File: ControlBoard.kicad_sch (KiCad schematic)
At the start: 9 parts, among them J1 Conn_02x07_Odd_Even, J2 Conn_02x07_Odd_Even, J3 Conn_02x03_Odd_Even, J5 Conn_01x06, J6 Conn_01x06, J7 Conn_01x02

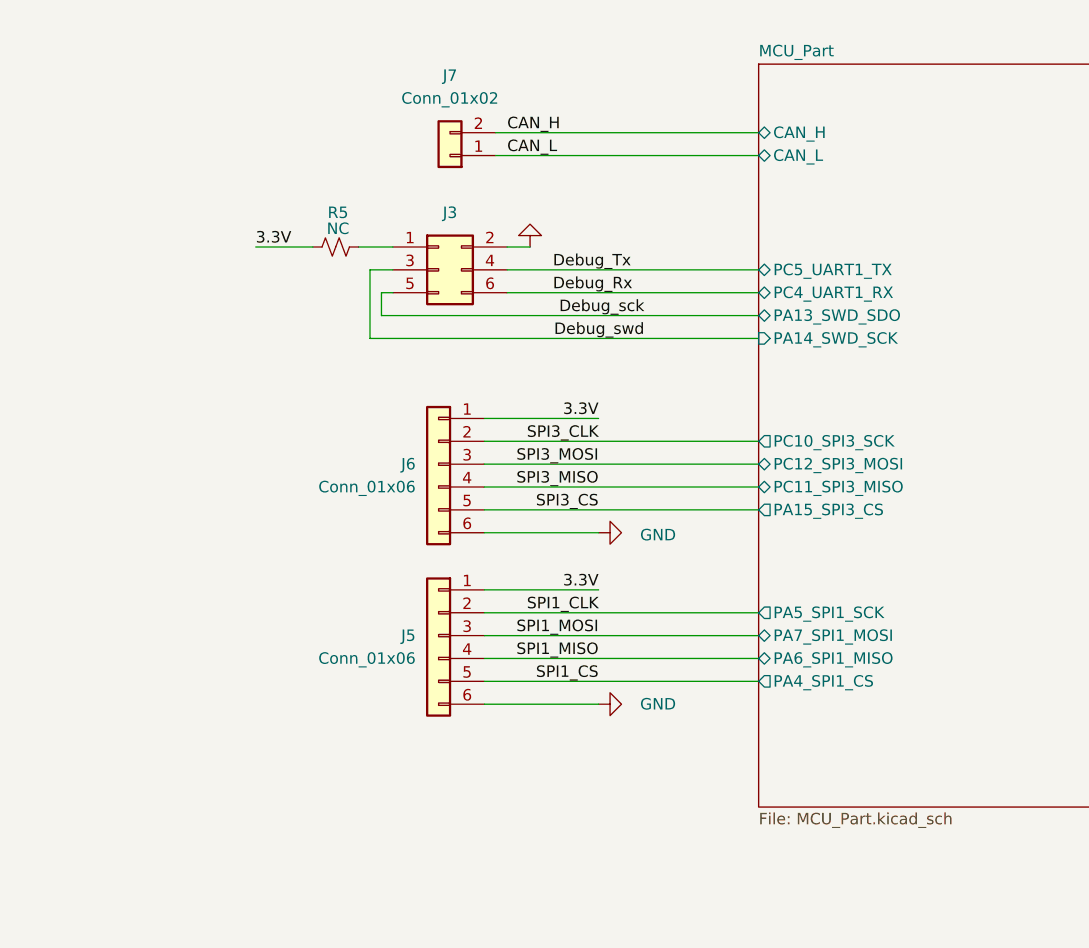
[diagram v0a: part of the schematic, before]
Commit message: 重新分配端子封装
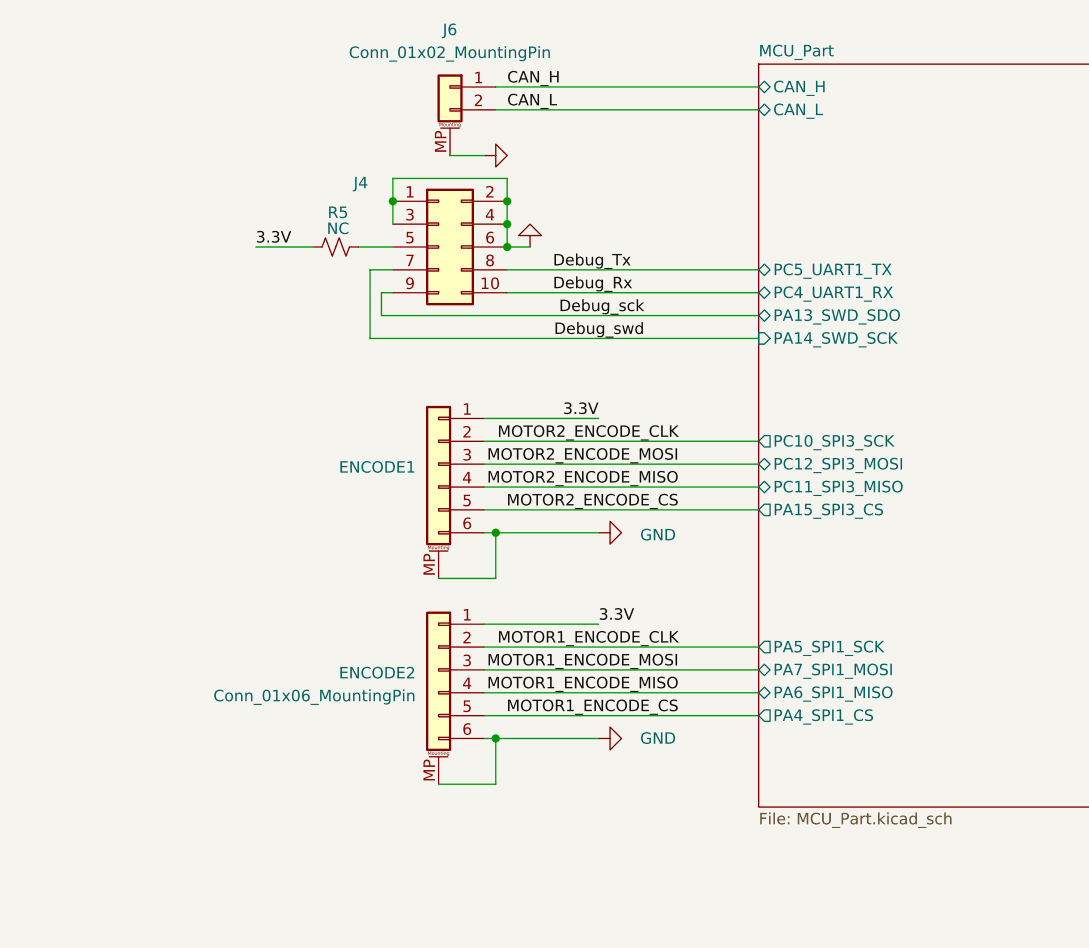
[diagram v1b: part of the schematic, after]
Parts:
- removed J3: Conn_02x03_Odd_Even, Connector_IDC:IDC-Header_2x03_P2.54mm_Vertical_SMD, symbol Connector_Generic:Conn_02x03_Odd_Even
- removed J5, J6: Conn_01x06, Connector_JST:JST_SH_BM06B-SRSS-TB_1x06-1MP_P1.00mm_Vertical, symbol Connector_Generic:Conn_01x06
- removed J7: Conn_01x02, Connector_JST:JST_SH_BM02B-SRSS-TB_1x02-1MP_P1.00mm_Vertical, symbol Connector_Generic:Conn_01x02
- added ENCODE1: ENCODE1, footprints:JST_SH_BM06B-SRSS-TB_1x06-1MP_P1.00mm_Horizontal, symbol Connector_Generic_MountingPin:Conn_01x06_MountingPin
- added ENCODE2: Conn_01x06_MountingPin, footprints:JST_SH_BM06B-SRSS-TB_1x06-1MP_P1.00mm_Horizontal, symbol Connector_Generic_MountingPin:Conn_01x06_MountingPin
- added J4: Conn_02x05_Odd_Even, footprints:Box_Head_1.27mm_SMD_Vertical_02x05, symbol Connector_Generic:Conn_02x05_Odd_Even
- added J6: Conn_01x02_MountingPin, footprints:JST_SH_BM02B-SRSS-TB_1x02-1MP_P1.00mm_Horizontal, symbol Connector_Generic_MountingPin:Conn_01x02_MountingPin
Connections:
- net 3.3V: now also ENCODE1.1 (Pin_1), ENCODE2.1 (Pin_1)
- net CAN_H: now also J6.1 (Pin_1)
- net CAN_L: now also J6.2 (Pin_2)
- net Debug_Rx: now also J4.10 (Pin_10)
- net Debug_Tx: now also J4.8 (Pin_8)
- net Debug_sck: now also J4.9 (Pin_9)
- net Debug_swd: now also J4.7 (Pin_7)
- net GND: now also ENCODE1.6 (Pin_6), ENCODE1.MP (MountPin), ENCODE2.6 (Pin_6), ENCODE2.MP (MountPin), J4.1 (Pin_1), J4.2 (Pin_2), J4.3 (Pin_3), J4.4 (Pin_4), J4.6 (Pin_6), J6.MP (MountPin)
- net at R5.2: now also J4.5 (Pin_5)
- new net MOTOR1_ENCODE_CLK: ENCODE2.2 (Pin_2)
- new net MOTOR1_ENCODE_CS: ENCODE2.5 (Pin_5)
- new net MOTOR1_ENCODE_MISO: ENCODE2.4 (Pin_4)
- new net MOTOR1_ENCODE_MOSI: ENCODE2.3 (Pin_3)
- new net MOTOR2_ENCODE_CLK: ENCODE1.2 (Pin_2)
- new net MOTOR2_ENCODE_CS: ENCODE1.5 (Pin_5)
- new net MOTOR2_ENCODE_MISO: ENCODE1.4 (Pin_4)
- new net MOTOR2_ENCODE_MOSI: ENCODE1.3 (Pin_3)

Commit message: 增加测试点
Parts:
- added TP10, TP11, TP12, TP13, TP14, TP15, TP16, TP17, TP18, TP19, TP20, TP21, TP22, TP23, TP24, TP25, TP26, TP27, TP28, TP29, TP3, TP30, TP31, TP32, TP33, TP34, TP35, TP36, TP37, TP38, TP39, TP4, TP40, TP41, TP42, TP43, TP44, TP45, TP46, TP47, TP48, TP5, TP6, TP7, TP8, TP9: TestPoint_Small, TestPoint:TestPoint_Pad_D1.0mm, symbol Connector:TestPoint_Small
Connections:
- net +3.3V: now also TP48.1
- net +5V: now also TP47.1
- net BusVoltage: now also TP22.1
- net CAN_H: now also J6.2 (Pin_2), TP4.1; no longer J6.1 (Pin_1)
- net CAN_L: now also J6.1 (Pin_1), TP3.1; no longer J6.2 (Pin_2)
- net MOTOR1_ADC_U: now also TP19.1
- net MOTOR1_ADC_V: now also TP20.1
- net MOTOR1_ADC_W: now also TP21.1
- net MOTOR1_BREAK: now also TP24.1
- net MOTOR1_ENCODE_CLK: now also TP9.1
- net MOTOR1_ENCODE_CS: now also TP12.1
- net MOTOR1_ENCODE_MISO: now also TP11.1
- net MOTOR1_ENCODE_MOSI: now also TP10.1
- net MOTOR1_U+: now also TP13.1, TP25.1
- net MOTOR1_U-: now also TP14.1, TP18.1, TP26.1, TP30.1
- net MOTOR1_V+: now also TP15.1, TP27.1
- net MOTOR1_V-: now also TP16.1, TP28.1
- net MOTOR1_W+: now also TP17.1, TP29.1
- net MOTOR2_ADC_U: now also TP37.1
- net MOTOR2_ADC_V: now also TP38.1
- net MOTOR2_ADC_W: now also TP39.1
- net MOTOR2_BREAK: now also TP40.1
- net MOTOR2_ENCODE_CLK: now also TP5.1
- net MOTOR2_ENCODE_CS: now also TP8.1
- net MOTOR2_ENCODE_MISO: now also TP7.1
- net MOTOR2_ENCODE_MOSI: now also TP6.1
- net MOTOR2_U+: now also TP31.1, TP41.1
- net MOTOR2_U-: now also TP32.1, TP36.1, TP42.1, TP46.1
- net MOTOR2_V+: now also TP33.1, TP43.1
- net MOTOR2_V-: now also TP34.1, TP44.1
- net MOTOR2_W+: now also TP35.1, TP45.1
- net busCurrent: now also TP23.1

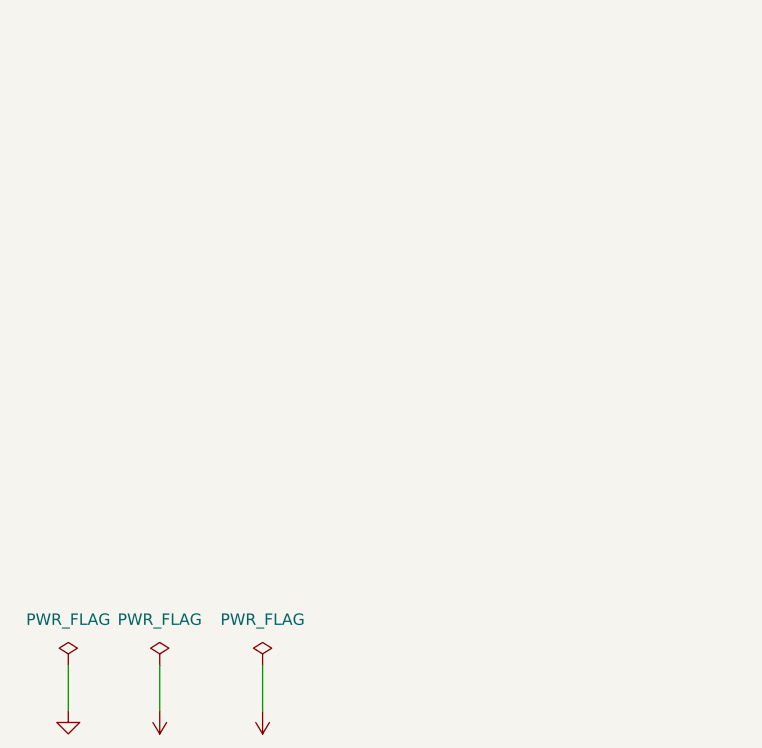
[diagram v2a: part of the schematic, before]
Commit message: 增加typeC接口
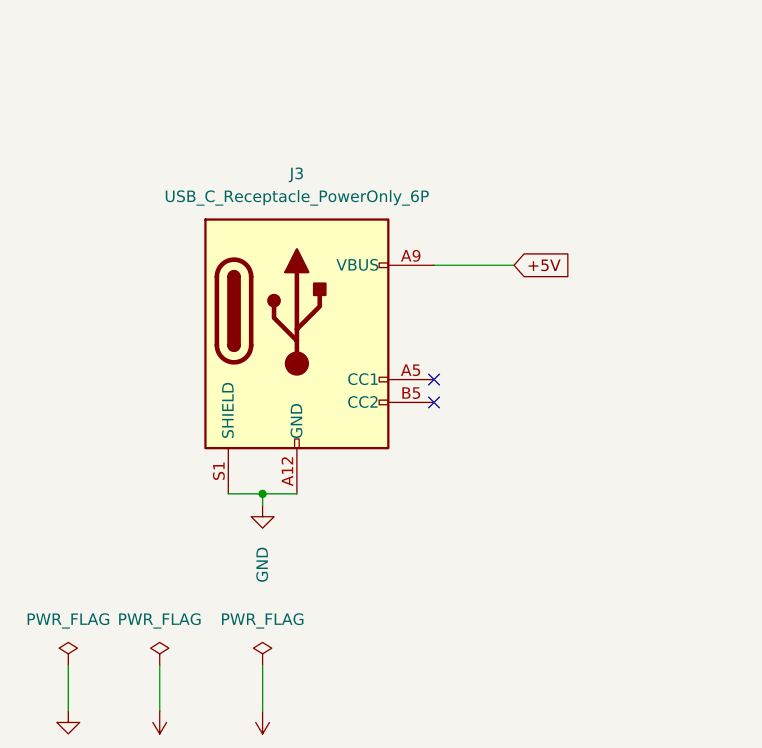
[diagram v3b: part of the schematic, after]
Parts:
- added J3: USB_C_Receptacle_PowerOnly_6P, Connector_USB:USB_C_Receptacle_GCT_USB4125-xx-x-0190_6P_TopMnt_Horizontal, symbol Connector:USB_C_Receptacle_PowerOnly_6P
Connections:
- net +5V: now also J3.A9 (VBUS), J3.B9 (VBUS)
- net GND: now also J3.A12 (GND), J3.B12 (GND), J3.S1 (SHIELD)
- no-connect marks 2 -> 4
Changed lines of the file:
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@@
 	)
 	(junction
+		(at 44.45 162.56)
+		(diameter 0)
+		(color 0 0 0 0)
+	)
+	(junction
 		(at 129.54 144.78)
 		(diameter 0)
@@
 	)
 	(no_connect
+		(at 63.5 149.86)
+	)
+	(no_connect
 		(at 231.14 109.22)
 	)
@@
 		(at 217.17 64.77)
 	)
+	(no_connect
+		(at 63.5 152.4)
+	)
 	(wire
 		(pts
@@
 	(wire
 		(pts
+			(xy 44.45 162.56) (xy 44.45 163.83)
+		)
+		(stroke
+			(width 0)
+			(type default)
+		)
+	)
+	(wire
+		(pts
 			(xy 190.5 99.06) (xy 193.04 99.06)
 		)
@@
 	(wire
 		(pts
+			(xy 44.45 162.56) (xy 48.26 162.56)
+		)
+		(stroke
+			(width 0)
+			(type default)
+		)
+	)
+	(wire
+		(pts
 			(xy 193.04 57.15) (xy 217.17 57.15)
 		)
@@
 	(wire
 		(pts
+			(xy 40.64 162.56) (xy 44.45 162.56)
+		)
+		(stroke
+			(width 0)
+			(type default)
+		)
+	)
+	(wire
+		(pts
 			(xy 87.63 64.77) (xy 74.93 64.77)
 		)
@@
 	(wire
 		(pts
+			(xy 63.5 137.16) (xy 72.39 137.16)
+		)
+		(stroke
+			(width 0)
+			(type default)
+		)
+	)
+	(wire
+		(pts
 			(xy 97.79 30.48) (xy 105.41 30.48)
 		)
@@
 	(global_label "+5V"
 		(shape input)
+		(at 72.39 137.16 0)
+		(fields_autoplaced yes)
+		(effects
+			(font
+				(size 1.27 1.27)
+			)
+			(justify left)
+		)
+		(property "Intersheetrefs" "${INTERSHEET_REFS}"
+			(at 79.2457 137.16 0)
+			(effects
+				(font
+					(size 1.27 1.27)
+				)
+				(justify left)
+				(hide yes)
+			)
+		)
+	)
+	(global_label "+5V"
+		(shape input)
 		(at 125.73 144.78 180)
 		(fields_autoplaced yes)
@@
 	)
 	(symbol
+		(lib_id "Connector:USB_C_Receptacle_PowerOnly_6P")
+		(at 48.26 144.78 0)
+		(unit 1)
+		(exclude_from_sim no)
+		(in_bom yes)
+		(on_board yes)
+		(dnp no)
+		(fields_autoplaced yes)
+		(property "Reference" "J3"
+			(at 48.26 127 0)
+			(effects
+				(font
+					(size 1.27 1.27)
+				)
+			)
+		)
+		(property "Value" "USB_C_Receptacle_PowerOnly_6P"
+			(at 48.26 129.54 0)
+			(effects
+				(font
+					(size 1.27 1.27)
+				)
+			)
+		)
+		(property "Footprint" "Connector_USB:USB_C_Receptacle_GCT_USB4125-xx-x-0190_6P_TopMnt_Horizontal"
+			(at 52.07 142.24 0)
+			(effects
+				(font
+					(size 1.27 1.27)
+				)
+				(hide yes)
+			)
+		)
+		(property "Datasheet" "https://www.usb.org/sites/default/files/documents/usb_type-c.zip"
+			(at 48.26 144.78 0)
+			(effects
+				(font
+					(size 1.27 1.27)
+				)
+				(hide yes)
+			)
+		)
+		(property "Description" "USB Power-Only 6P Type-C Receptacle connector"
+			(at 48.26 144.78 0)
+			(effects
+				(font
+					(size 1.27 1.27)
+				)
+				(hide yes)
+			)
+		)
+		(pin "S1"
+		)
+		(pin "A12"
+		)
+		(pin "B12"
+		)
+		(pin "A9"
+		)
+		(pin "B9"
+		)
+		(pin "A5"
+		)
+		(pin "B5"
+		)
+		(instances
+			(project "ControlBoard"
+				(path "/bfd4cee4-1f26-4ec9-a630-f44d434f4dbf"
+					(reference "J3")
+					(unit 1)
+				)
+			)
+		)
+	)
+	(symbol
 		(lib_id "Connector:TestPoint_Small")
 		(at 99.06 72.39 0)
@@
 					(unit 1)
 				)
+			)
+		)
+	)
+	(symbol
+		(lib_id "power:GND")
+		(at 44.45 163.83 0)
+		(unit 1)
+		(exclude_from_sim no)
+		(in_bom yes)
+		(on_board yes)
+		(dnp no)
+		(property "Reference" "#PWR036"
+			(at 44.45 170.18 0)
+			(effects
+				(font
+					(size 1.27 1.27)
+				)
+				(hide yes)
+			)
+		)
+		(property "Value" "GND"
+			(at 44.45 170.434 90)
+			(effects
+				(font
+					(size 1.27 1.27)
+				)
+			)
+		)
+		(property "Footprint" ""
+			(at 44.45 163.83 0)
+			(effects
+				(font
+					(size 1.27 1.27)
+				)
+				(hide yes)
+			)
+		)
+		(property "Datasheet" ""
+			(at 44.45 163.83 0)
+			(effects
+				(font
+					(size 1.27 1.27)
+				)
+				(hide yes)
+			)
+		)
+		(property "Description" "Power symbol creates a global label with name \"GND\" , ground"
+			(at 44.45 163.83 0)
+			(effects
+				(font
+					(size 1.27 1.27)
+				)
+				(hide yes)
+			)
+		)
+		(pin "1"
+		)
+		(instances
+			(project "ControlBoard"
+				(path "/bfd4cee4-1f26-4ec9-a630-f44d434f4dbf"
+					(reference "#PWR036")
+					(unit 1)
+				)

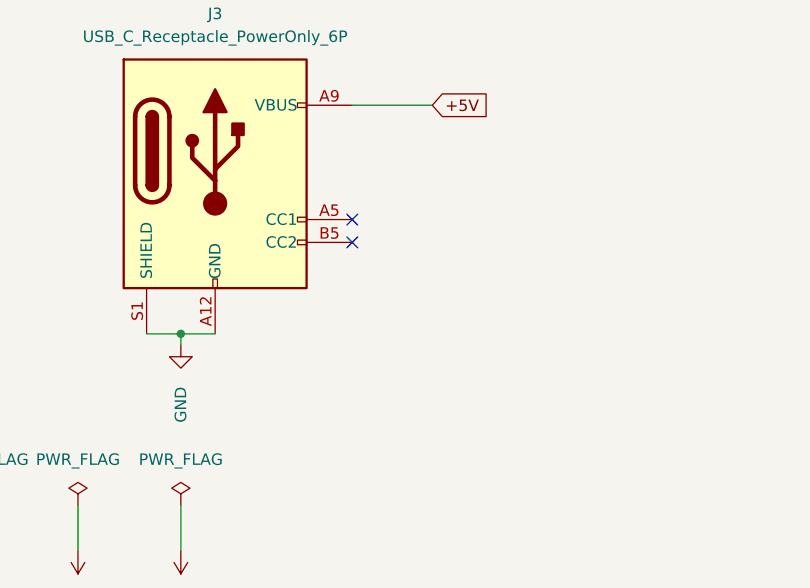
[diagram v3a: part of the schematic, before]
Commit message: 优化Type-C电路
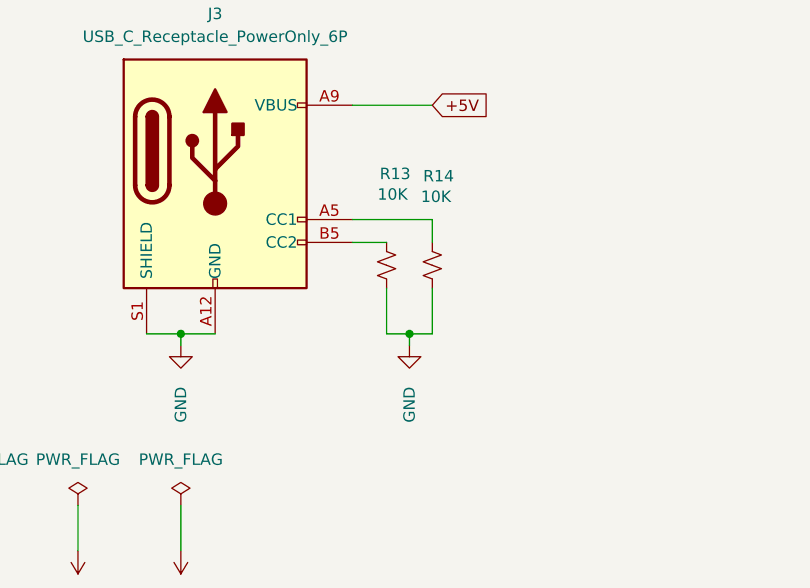
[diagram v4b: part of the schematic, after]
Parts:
- added R13, R14: 10K, Resistor_SMD:R_0603_1608Metric_Pad0.98x0.95mm_HandSolder, symbol Device:R_Small_US
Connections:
- net GND: now also R13.2, R14.2
- net at J3.A5 (CC1): now also R14.1
- net at J3.B5 (CC2): now also R13.1
- no-connect marks 4 -> 2

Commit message: 优化PCB布线20250919
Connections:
- net MOTOR1_U-: no longer J1.12 (Pin_12), TP18.1, TP30.1
- net MOTOR2_U-: no longer J2.12 (Pin_12), TP36.1, TP46.1
- new net MOTOR1_W-: J1.12 (Pin_12), TP18.1, TP30.1
- new net MOTOR2_W-: J2.12 (Pin_12), TP36.1, TP46.1
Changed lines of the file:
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@@
 		)
 	)
-	(label "MOTOR1_U-"
+	(label "MOTOR1_W-"
 		(at 210.82 41.91 180)
 		(effects
@@
 		)
 	)
-	(label "MOTOR1_U-"
+	(label "MOTOR1_W-"
 		(at 251.46 62.23 180)
 		(effects
@@
 		)
 	)
-	(label "MOTOR2_U-"
+	(label "MOTOR2_W-"
 		(at 210.82 85.09 180)
 		(effects
@@
 		)
 	)
-	(label "MOTOR2_U-"
+	(label "MOTOR2_W-"
 		(at 254 106.68 180)
 		(effects

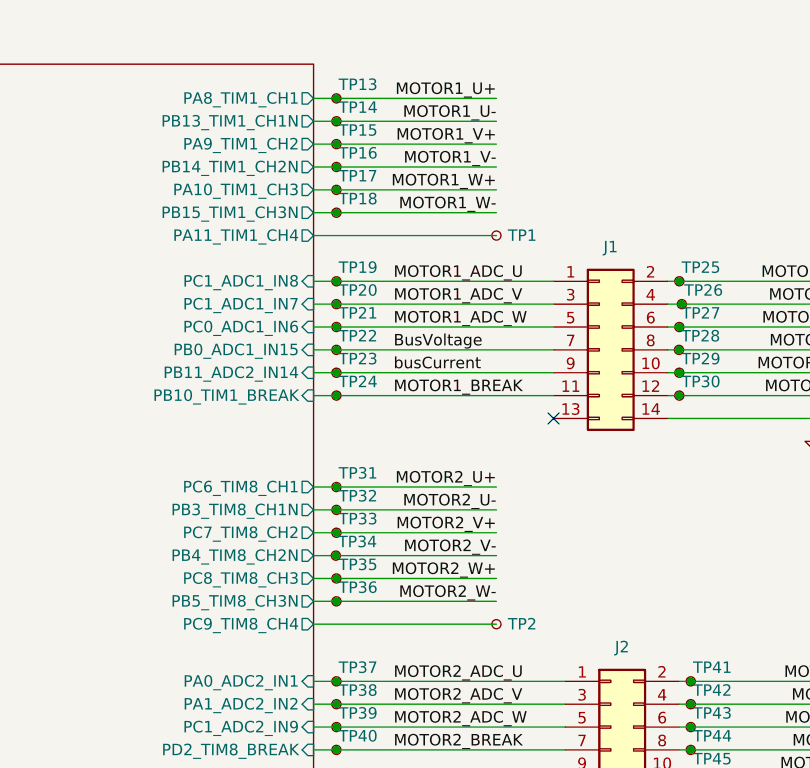
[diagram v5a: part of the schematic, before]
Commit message: 信号线布线完成
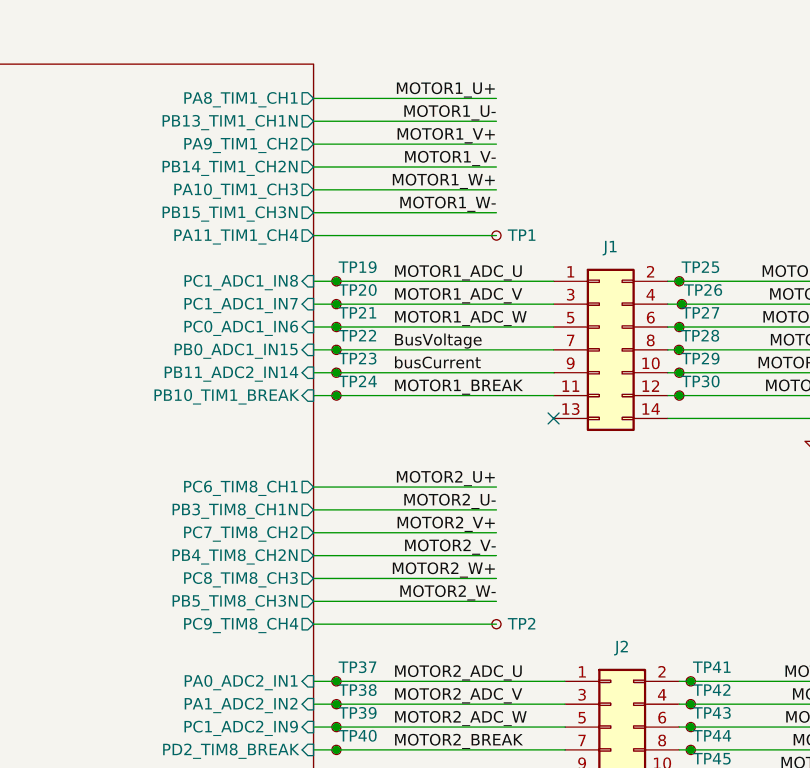
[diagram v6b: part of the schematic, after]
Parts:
- removed TP13, TP14, TP15, TP16, TP17, TP18, TP31, TP32, TP33, TP34, TP35, TP36: TestPoint_Small, TestPoint:TestPoint_Pad_D1.0mm, symbol Connector:TestPoint_Small
